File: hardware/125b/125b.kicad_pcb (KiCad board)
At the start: 2 copper layers, 59 x 75 mm, 58 parts, among them J1 Guitar in, J10 Barrel_Jack, J11 NRJ6HF, J2 fsw pin 7, J3 fsw pin 2, J4 fsw pin 7, J5 fsw pin 5, J6 fsw pin 6, J7 fsw pin 3, J8 fsw pin 4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

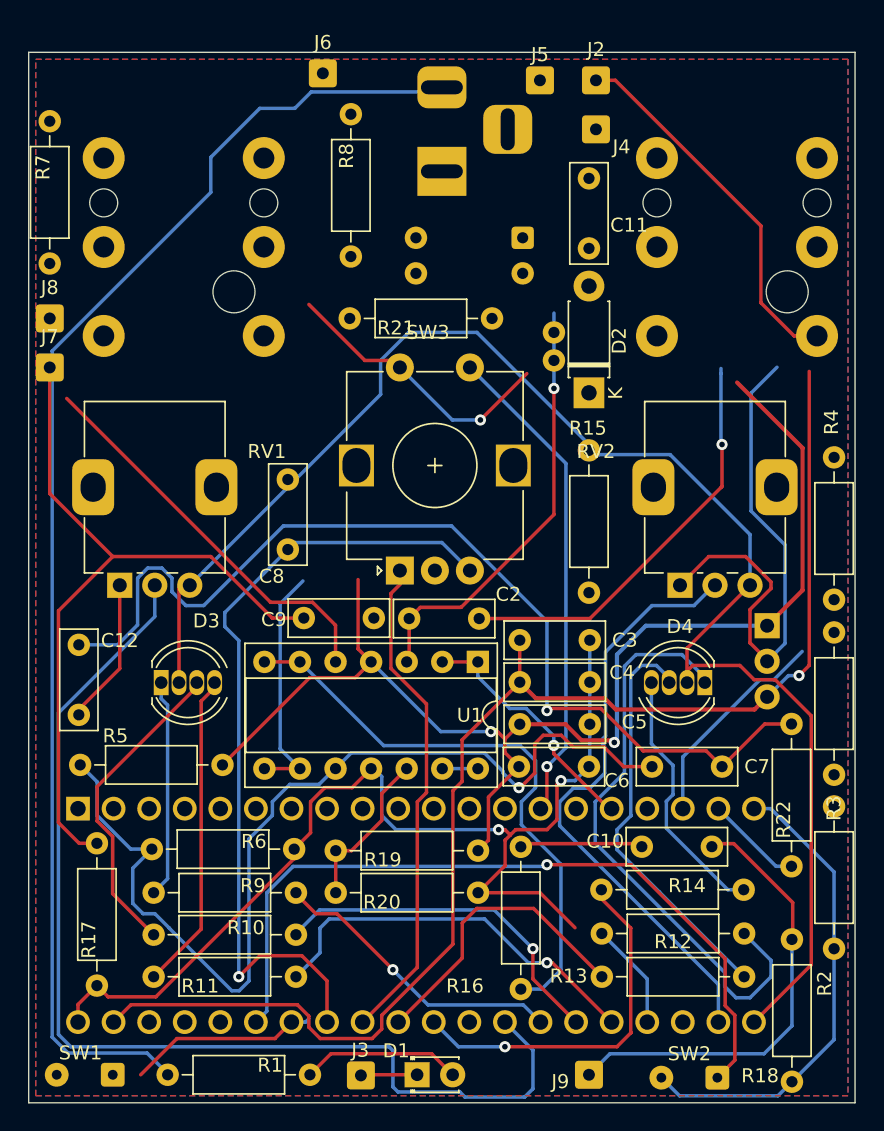
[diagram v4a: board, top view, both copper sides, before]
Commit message: Fix unconnected items and update footprints
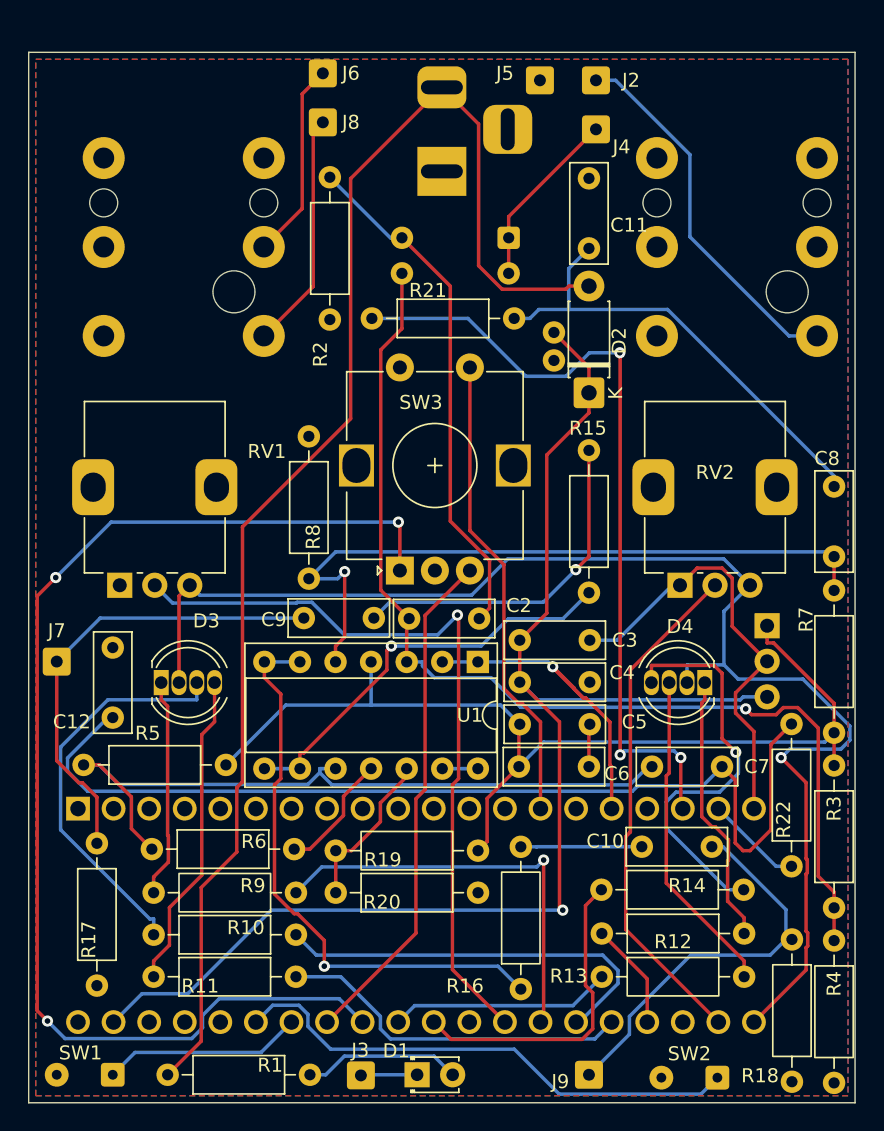
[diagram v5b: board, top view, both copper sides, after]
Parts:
- moved R7 65.3 mm to (155.5, 83.6)
- moved R2 57.6 mm to (119.5, 43.9)
- moved C8 39.3 mm to (155.5, 66.0), turned to -90 degrees
- moved R4 34.5 mm to (155.5, 98.4)
- moved R8 33.3 mm to (118.0, 72.6), turned to 90 degrees
- moved J8 24.0 mm to (119.0, 40.0)
- moved J7 21.0 mm to (100.0, 78.5)
- moved C12 5.38 mm to (104.0, 77.5), turned to -90 degrees
- moved R21 1.58 mm to (122.5, 54.0)
- moved SW4 1.00 mm to (132.3, 48.2)
- moved R3 0.66 mm to (155.5, 85.9), turned to -90 degrees
- moved R5 0.25 mm to (112.1, 85.9)
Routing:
- net GND: track 179.9 -> 43.4 mm, vias 3 -> 0
- net /ENC_A: track 36.3 -> 87.5 mm, vias 0 -> 3
- net Net-(U1A-+): track 31.0 -> 76.8 mm
- net /Left out: track 15.3 -> 57.2 mm, vias 0 -> 3
- net Net-(C11-Pad2): track 0.00 -> 33.7 mm
- net Net-(C9-Pad1): track 0.00 -> 24.8 mm, vias 0 -> 1
- net Net-(A1-ADC_6): track 78.0 -> 54.5 mm, vias 0 -> 1
- net Net-(D4-RK): track 42.8 -> 19.5 mm
- net Net-(U1B-+): track 28.5 -> 50.3 mm, vias 0 -> 1
- net Net-(J7-Pin_1): track 54.8 -> 33.2 mm
- net /ENC_B: track 57.4 -> 36.5 mm, vias 1 -> 0
- net Net-(U1C-+): track 72.0 -> 52.5 mm, vias 1 -> 0
- net Net-(A1-SAI2_SCK): track 55.2 -> 37.1 mm, vias 1 -> 0
- net Net-(J8-Pin_1): track 0.00 -> 17.0 mm
- net +5V: track 88.4 -> 72.4 mm, vias 2 -> 0
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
